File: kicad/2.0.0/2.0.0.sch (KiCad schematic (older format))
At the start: 55 parts, among them J1 DIFFX, J2 DIFFY, J3 POWER, J4 SUM, U1 OPA2197IDR, U2 OPA2197IDR, U3 LM317, U4 LM337, U5 OPA2197IDR, U6 OPA197IDR

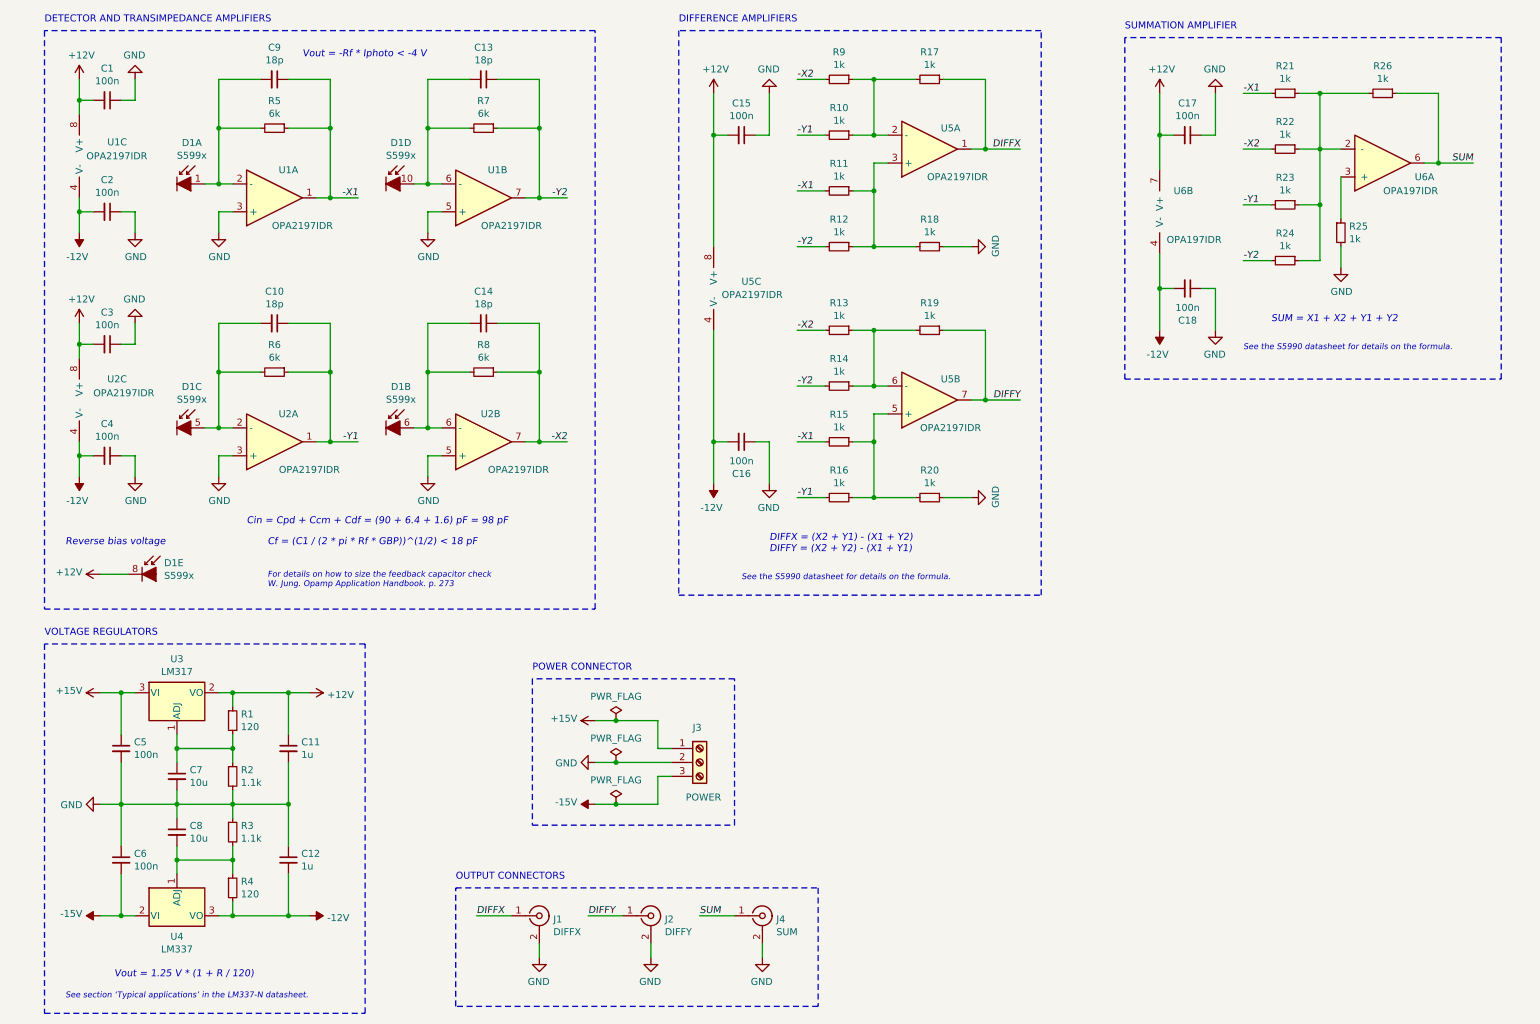
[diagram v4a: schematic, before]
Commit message: separated 2.0.0 using hierarchical sheets, added voltage reference to 2.0.0
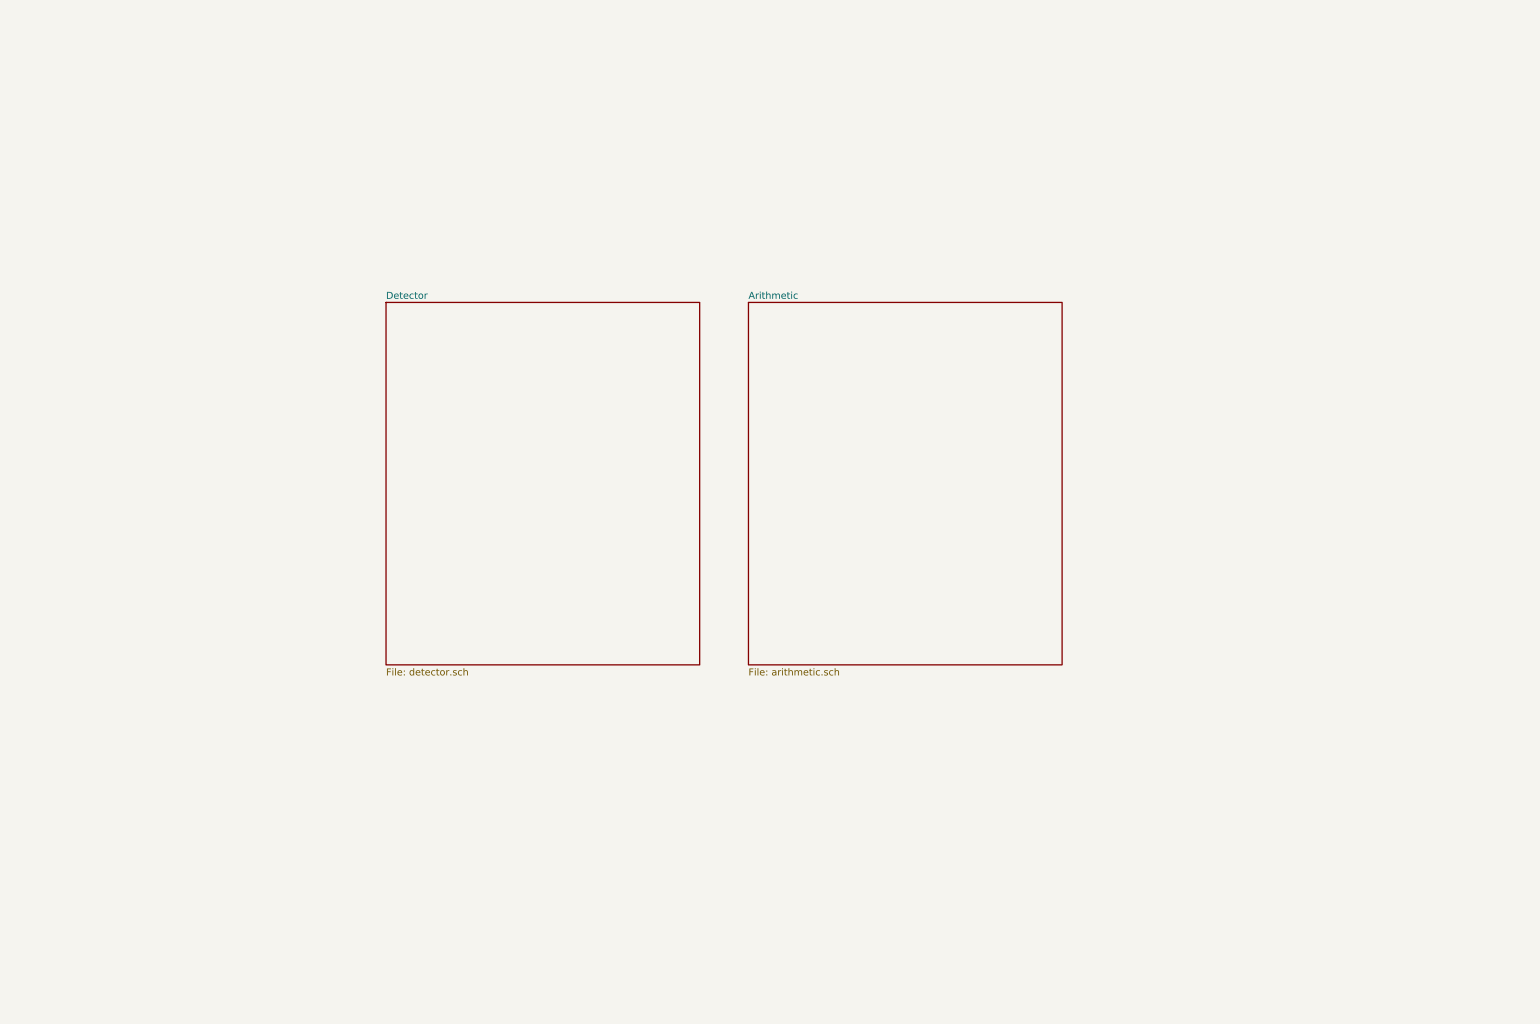
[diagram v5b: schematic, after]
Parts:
- removed C1, C15, C16, C17, C18, C2, C3, C4, C5, C6: 100n, Capacitor_SMD:C_0603_1608Metric, symbol Device:C_Small
- removed C10, C13, C14, C9: 18p, Capacitor_SMD:C_0603_1608Metric, symbol Device:C_Small
- removed C11, C12: 1u, Capacitor_SMD:C_0603_1608Metric, symbol Device:C_Small
- removed C7, C8: 10u, Capacitor_SMD:C_1206_3216Metric, symbol Device:C_Small
- removed D1: S599x, Sensor_Optical_Position:S5990, symbol Sensor_Optical_Position:S599x
- removed J1: DIFFX, Connector_SMA:SMA_Molex_73251-2120_EdgeMount, symbol Connector:Conn_Coaxial
- removed J2: DIFFY, Connector_SMA:SMA_Molex_73251-2120_EdgeMount, symbol Connector:Conn_Coaxial
- removed J3: POWER, TerminalBlock_TE-Connectivity:TerminalBlock_TE_282834-3_1x03_P2.54mm_Horizontal, symbol Connector:Screw_Terminal_01x03
- removed J4: SUM, Connector_SMA:SMA_Molex_73251-2120_EdgeMount, symbol Connector:Conn_Coaxial
- removed R1, R4: 120, Resistor_SMD:R_0603_1608Metric, symbol Device:R_Small
- removed R10, R11, R12, R13, R14, R15, R16, R17, R18, R19, R20, R21, R22, R23, R24, R25, R26, R9: 1k, Resistor_SMD:R_0603_1608Metric, symbol Device:R_Small
- removed R2, R3: 1.1k, Resistor_SMD:R_0603_1608Metric, symbol Device:R_Small
- removed R5, R6, R7, R8: 6k, Resistor_SMD:R_0603_1608Metric, symbol Device:R_Small
- removed U1, U2, U5: OPA2197IDR, Package_SO:SOIC-8_3.9x4.9mm_P1.27mm, symbol Amplifier_Operational:OPA2197IDR
- removed U3: LM317, Package_TO_SOT_SMD:SOT-223-3_TabPin2, symbol Regulator_Linear:LM317_3PinPackage
- removed U4: LM337, Package_TO_SOT_SMD:SOT-223-3_TabPin2, symbol Regulator_Linear:LM337_SOT223
- removed U6: OPA197IDR, Package_SO:SOIC-8_3.9x4.9mm_P1.27mm, symbol Amplifier_Operational:OPA197IDR
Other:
- note removed: "Cf = (C1 / (2 * pi * Rf * GBP))^(1/2) < 18 pF"
- note removed: "Cin = Cpd + Ccm + Cdf = (90 + 6.4 + 1.6) pF = 98 pF"
- note removed: "DETECTOR AND TRANSIMPEDANCE AMPLIFIERS"
- note removed: "DIFFERENCE AMPLIFIERS"
- note removed: "DIFFX = (X2 + Y1) - (X1 + Y2)\nDIFFY = (X2 + Y2) - (X1 + Y1)"
- note removed: "For details on how to size the feedback capacitor check\nW. Jung. Opamp Application Handbook. p. 273"
- note removed: "OUTPUT CONNECTORS"
- note removed: "POWER CONNECTOR"
- note removed: "Reverse bias voltage"
- note removed: "SUM = X1 + X2 + Y1 + Y2"
- note removed: "SUMMATION AMPLIFIER"
- note removed: "See section ‘Typical applications’ in the LM337-N datasheet."
- note removed: "See the S5990 datasheet for details on the formula."
- note removed: "VOLTAGE REGULATORS"
- note removed: "Vout = -Rf * Iphoto < -4 V"
- note removed: "Vout = 1.25 V * (1 + R / 120)"

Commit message: added power leds and test points to 2.0.0
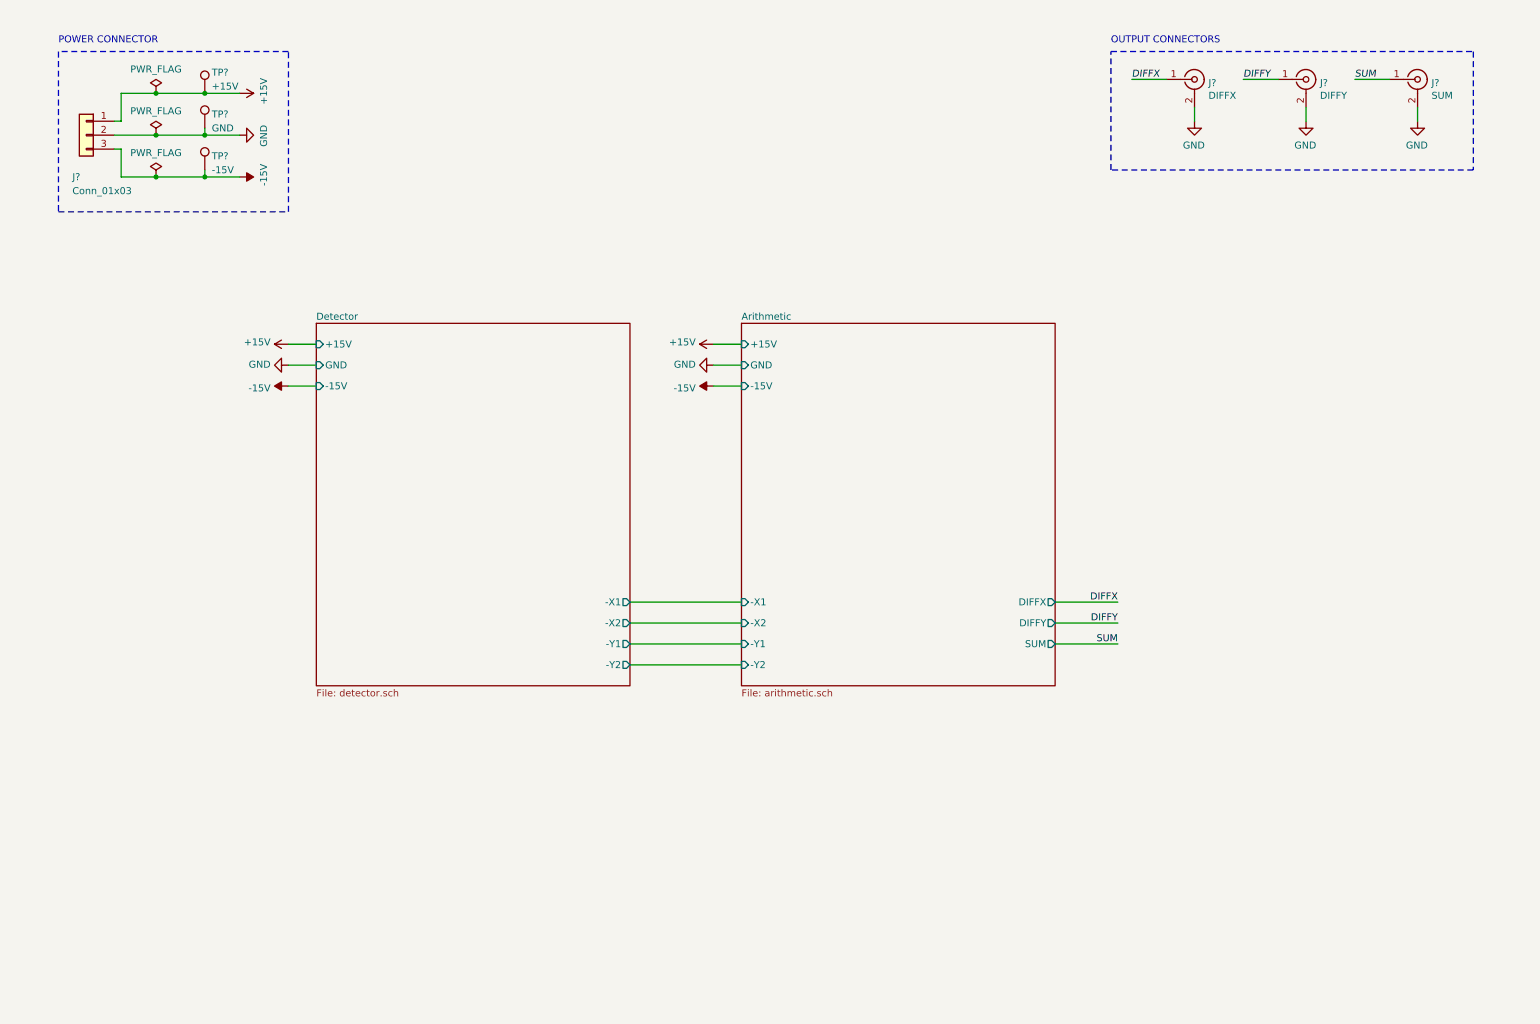
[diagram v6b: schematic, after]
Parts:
- added J?: Conn_01x03, symbol Connector_Generic:Conn_01x03
- added J?: DIFFX, Connector_SMA:SMA_Molex_73251-2120_EdgeMount, symbol Connector:Conn_Coaxial
- added J?: DIFFY, Connector_SMA:SMA_Molex_73251-2120_EdgeMount, symbol Connector:Conn_Coaxial
- added J?: SUM, Connector_SMA:SMA_Molex_73251-2120_EdgeMount, symbol Connector:Conn_Coaxial
- added TP?: +15V, symbol Connector:TestPoint
- added TP?: -15V, symbol Connector:TestPoint
- added TP?: GND, symbol Connector:TestPoint
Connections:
- new net +15V: J?.1 (Pin_1), TP?.1
- new net -15V: J?.3 (Pin_3), TP?.1
- new net DIFFX: J?.1 (In)
- new net DIFFY: J?.1 (In)
- new net GND: J?.2 (Ext), J?.2 (Ext), J?.2 (Ext), J?.2 (Pin_2), TP?.1
- new net SUM: J?.1 (In)
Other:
- note added: "OUTPUT CONNECTORS"
- note added: "POWER CONNECTOR"
